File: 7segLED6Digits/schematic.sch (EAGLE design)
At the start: 43 parts, among them Q1 MPSA56-TO92, Q2 MPSA56-TO92, Q3 MPSA56-TO92, Q4 MPSA56-TO92, Q5 MPSA56-TO92, Q6 MPSA56-TO92, T1 2SC1815, T2 2SC1815, T3 2SC1815, T4 2SC1815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

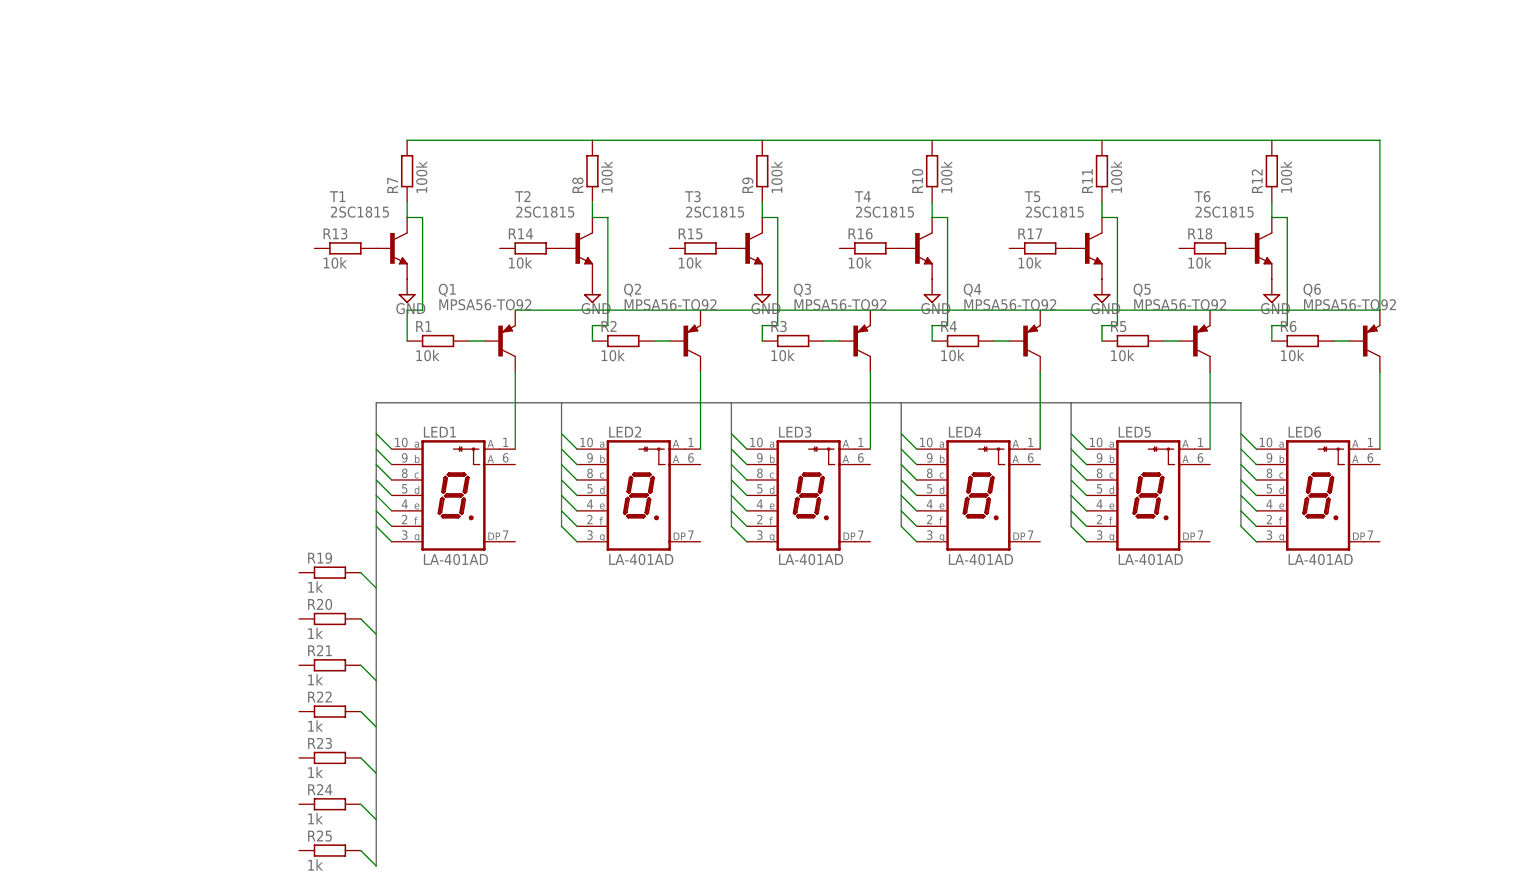
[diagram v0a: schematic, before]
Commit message: PNPのベース電圧分圧用抵抗追加 ボード図追加
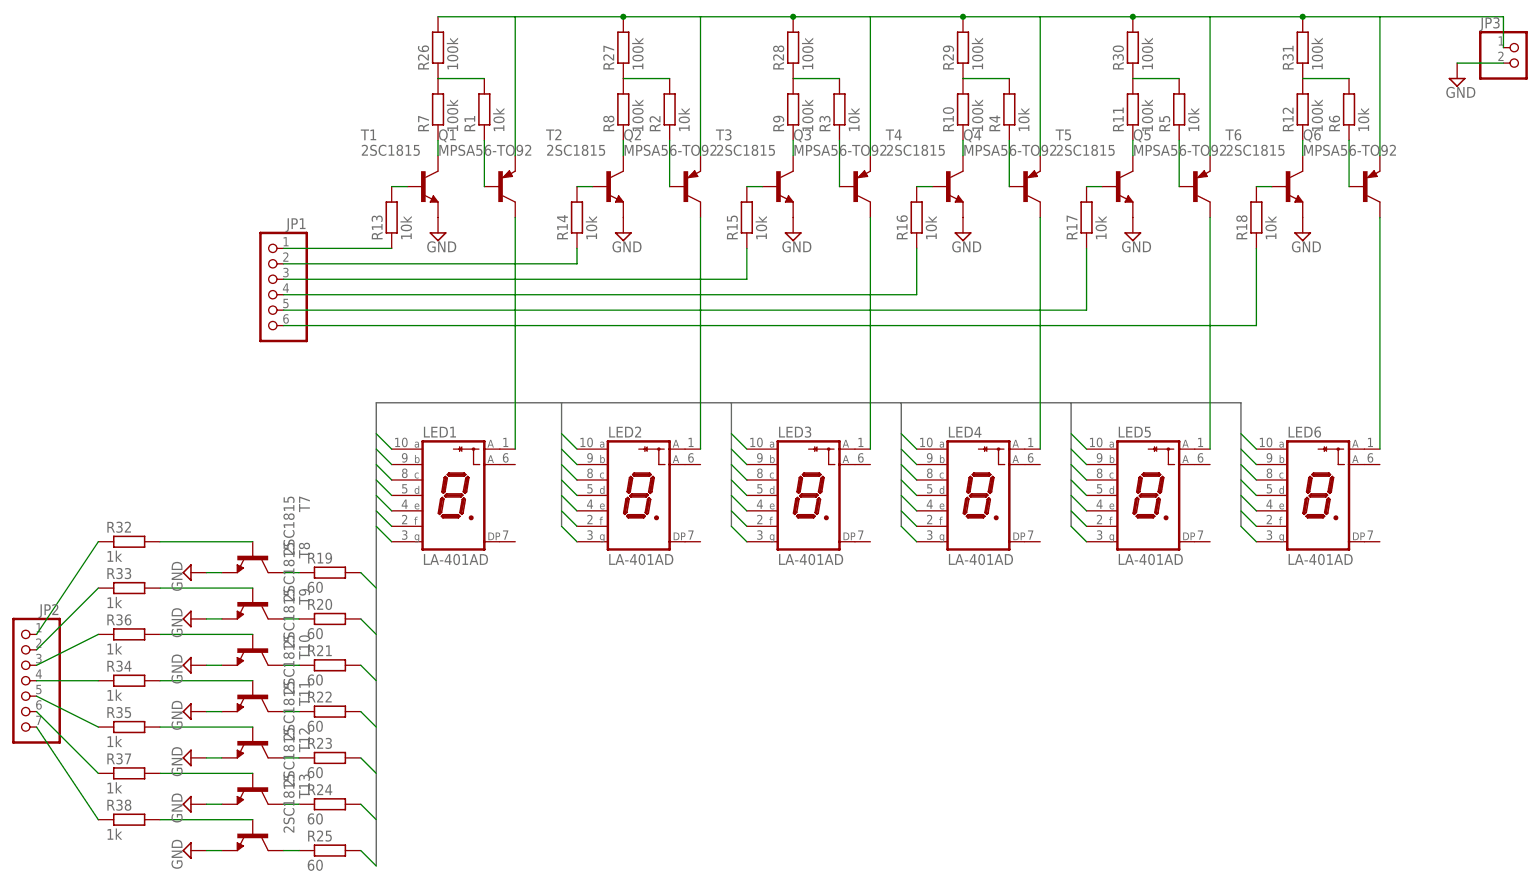
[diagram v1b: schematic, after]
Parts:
- added JP1: (no value), pinhead:PINHD-1X6
- added JP2: (no value), pinhead:PINHD-1X7
- added JP3: (no value), pinhead:PINHD-1X2
- added R26, R27, R28, R29, R30, R31: 100k, resistor:R-EU_0204/5
- added R32, R33, R34, R35, R36, R37, R38: 1k, resistor:R-EU_0204/5
- added T10, T11, T12, T13, T7, T8, T9: 2SC1815, transistor:2SC1815
- R19, R20, R21, R22, R23, R24, R25: value 1k -> 60
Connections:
- removed net N$15 (its old number): Q4.B, R4.2
- removed net N$17 (its old number): Q5.B, R5.2
- removed net N$18 (its old number): Q6.B, R6.2
- removed net N$20 (its old number): R11.1, R5.1, T5.C
- removed net N$22 (its old number): R2.1, R8.1, T2.C
- removed net N$23 (its old number): R3.1, R9.1, T3.C
- new net N$1: R2.2, R27.1, R8.2
- new net N$2: Q2.B, R2.1
- new net N$26: R19.1, T7.C
- new net N$27: R25.1, T13.C
- new net N$28: R24.1, T12.C
- new net N$29: R23.1, T11.C
- new net N$3: Q4.B, R4.1
- new net N$30: R22.1, T10.C
- new net N$31: R21.1, T9.C
- new net N$32: R7.1, T1.C
- new net N$33: R8.1, T2.C
- new net N$34: R9.1, T3.C
- new net N$35: R12.1, T6.C
- new net N$36: R11.1, T5.C
- new net N$37: R10.1, T4.C
- new net N$38: R20.1, T8.C
- new net N$39: R32.2, T7.B
- new net N$4: R11.2, R30.1, R5.2
- new net N$40: R33.2, T8.B
- new net N$41: R36.2, T9.B
- new net N$42: R34.2, T10.B
- new net N$43: R35.2, T11.B
- new net N$44: R37.2, T12.B
- new net N$45: R38.2, T13.B
- new net N$46: JP2.1, R32.1
- new net N$47: JP2.2, R33.1
- new net N$48: JP2.3, R36.1
- new net N$49: JP2.4, R34.1
- new net N$5: Q5.B, R5.1
- new net N$50: JP2.5, R35.1
- new net N$51: JP2.6, R37.1
- new net N$52: JP2.7, R38.1
- new net N$53: JP1.1, R13.1
- new net N$54: JP1.2, R14.1
- new net N$55: JP1.3, R15.1
- new net N$56: JP1.4, R16.1
- new net N$57: JP1.5, R17.1
- new net N$58: JP1.6, R18.1
- new net N$6: Q6.B, R6.1
- net GND: now also JP3.2, T10.E, T11.E, T12.E, T13.E, T7.E, T8.E, T9.E
- net N$10: now also R28.1, R3.2, R9.2; no longer Q2.B, R2.2
- net N$13: now also R3.1; no longer R3.2
- net N$21: now also R1.2, R26.1, R7.2; no longer R1.1, R7.1, T1.C
- net N$24: now also R10.2, R29.1, R4.2; no longer R10.1, R4.1, T4.C
- net N$25: now also R12.2, R31.1, R6.2; no longer R12.1, R6.1, T6.C
- net N$7: now also JP3.1, Q2.E, Q3.E, Q4.E, Q5.E, R26.2, R27.2, R28.2, R29.2, R30.2, R31.2; no longer R7.2
- net N$9: now also R1.1; no longer R1.2
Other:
- moved on the sheet: Q1, Q2, Q3, Q4, Q5, Q6, R1, R10, R11, R12, R13, R14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
